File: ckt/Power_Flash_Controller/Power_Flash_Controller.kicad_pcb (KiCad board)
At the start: 2 copper layers, 93 x 67.5 mm, 32 parts, among them J2 Screw_Terminal_01x03, J3 Screw_Terminal_01x03, J4 Screw_Terminal_01x03, K4 SANYOU_SRD_Form_C, K5 SANYOU_SRD_Form_C, K6 SANYOU_SRD_Form_C, M2 MountingHole_2.2mm_M2, Q1 BC857, Q2 BC857, Q3 BC857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

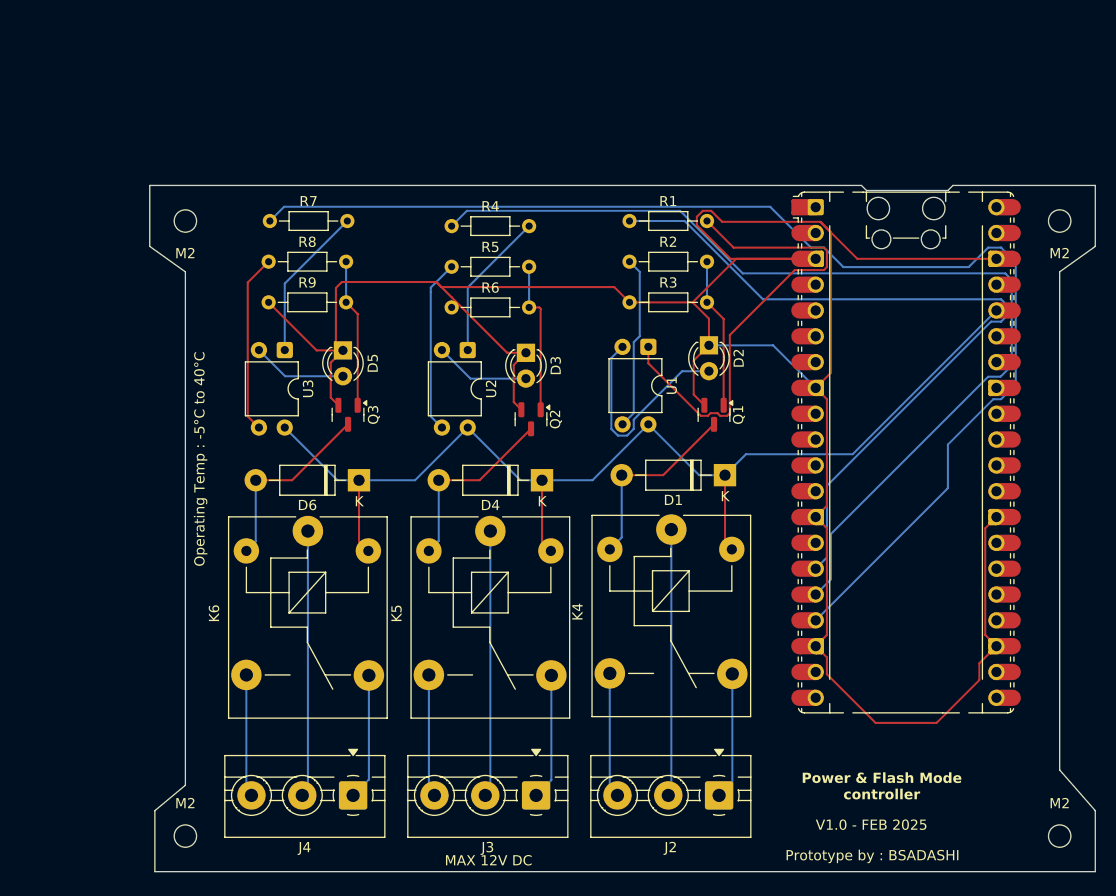
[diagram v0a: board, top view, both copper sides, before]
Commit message: rounded the paths and added GND fill layer
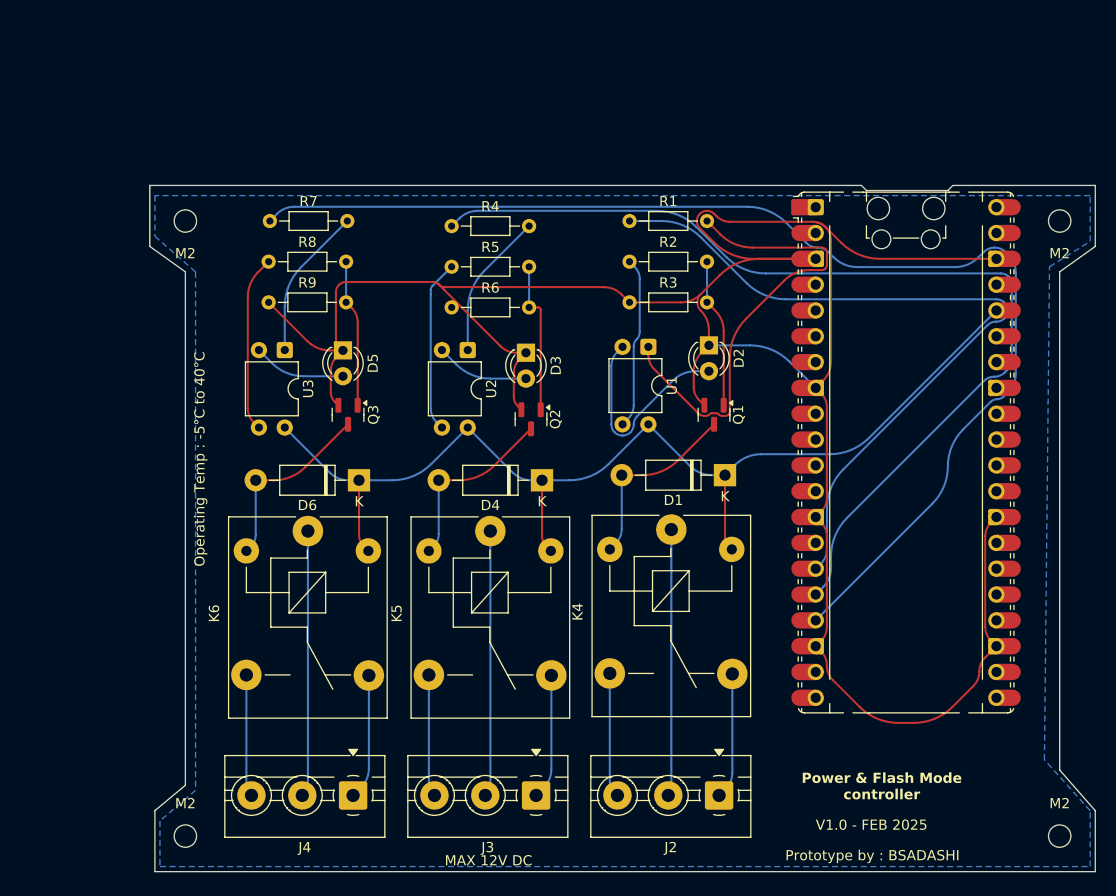
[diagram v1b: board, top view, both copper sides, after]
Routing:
- net GND: track 243.1 -> 238.4 mm
- net /IN3: track 121.6 -> 119.8 mm
- net /PPBus_3p3H: track 109.7 -> 108.0 mm
- net /IN2: track 98.2 -> 96.8 mm
- net /IN1: track 74.9 -> 73.8 mm
- net Net-(R1-Pad2): track 46.7 -> 45.7 mm
- net Net-(D2-A): track 21.6 -> 21.0 mm
- added copper zone on B.Cu, net GND

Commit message: Added connections for Ammeter and Voltmeter
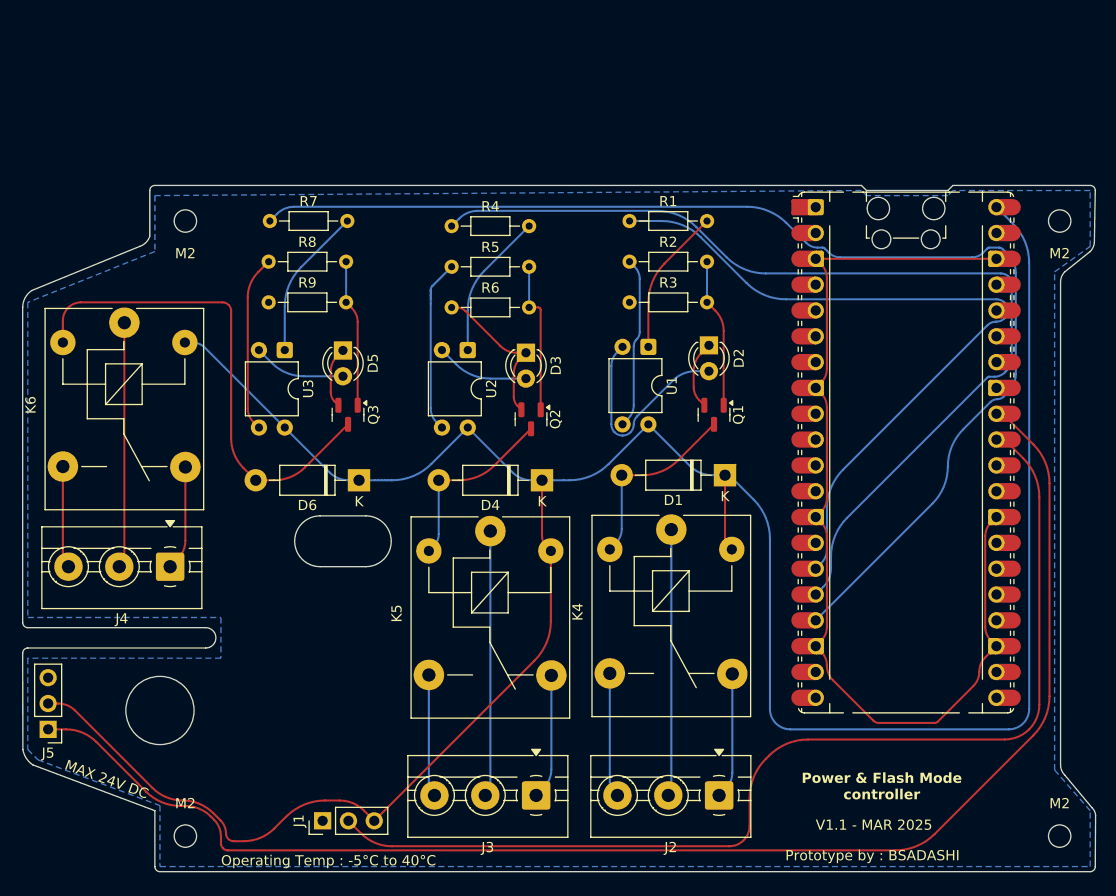
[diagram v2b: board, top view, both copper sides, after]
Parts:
- added J1: Conn_01x03, Connector_PinHeader_2.54mm:PinHeader_1x03_P2.54mm_Vertical, F.Cu at (114.5, 131.0)
- added J5: Conn_01x03, Connector_PinHeader_2.54mm:PinHeader_1x03_P2.54mm_Vertical, F.Cu at (87.5, 122.0)
- moved J4 28.8 mm to (99.5, 106.0)
- moved K6 27.3 mm to (95.0, 82.0)
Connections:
- A1 pad 31: unconnected-(A1-GPIO26_ADC0-Pad31) -> /ADC2Amtr
- A1 pad 32: unconnected-(A1-GPIO27_ADC1-Pad32) -> /ADC2Vmtr
- A1 pad 36: /PPBus_3p3H -> unconnected-(A1-3V3-Pad36)
- A1 pad 40: unconnected-(A1-VBUS-Pad40) -> /PPBus_5p0H
- D1 pad 1: /PPBus_3p3H -> /PPBus_5p0H
- D4 pad 1: /PPBus_3p3H -> /PPBus_5p0H
- D6 pad 1: /PPBus_3p3H -> /PPBus_5p0H
- K4 pad 5: /PPBus_3p3H -> /PPBus_5p0H
- K5 pad 5: /PPBus_3p3H -> /PPBus_5p0H
- K6 pad 5: /PPBus_3p3H -> /PPBus_5p0H
- U1 pad 4: /PPBus_3p3H -> /PPBus_5p0H
- U2 pad 4: /PPBus_3p3H -> /PPBus_5p0H
- U3 pad 4: /PPBus_3p3H -> /PPBus_5p0H
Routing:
- net /PPBus_5p0H: track 0.00 -> 258.2 mm
- net /ADC2Vmtr: track 0.00 -> 140.9 mm
- net GND: track 238.4 -> 125.3 mm
- net /PPBus_3p3H: track 108.0 -> 0.00 mm
- net /ADC2Amtr: track 0.00 -> 104.9 mm
- net Net-(R1-Pad2): track 45.7 -> 14.5 mm
- net Net-(D6-A): track 18.4 -> 48.8 mm
- net /R_NC3: track 12.3 -> 10.3 mm
- net /R_COM3: track 26.2 -> 24.2 mm
- net /R_NO3: track 12.0 -> 10.0 mm
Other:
- board size 93 x 67.5 mm -> 105.5 x 67.5 mm
- board text added: "MAX 24V DC"
- board text added: "V1.1 - MAR 2025"
- board text removed: "MAX 12V DC"
- board text removed: "V1.0 - FEB 2025"

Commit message: added relay no.4 and oled display mount, option for pwm fan and ammeter, voltmeter
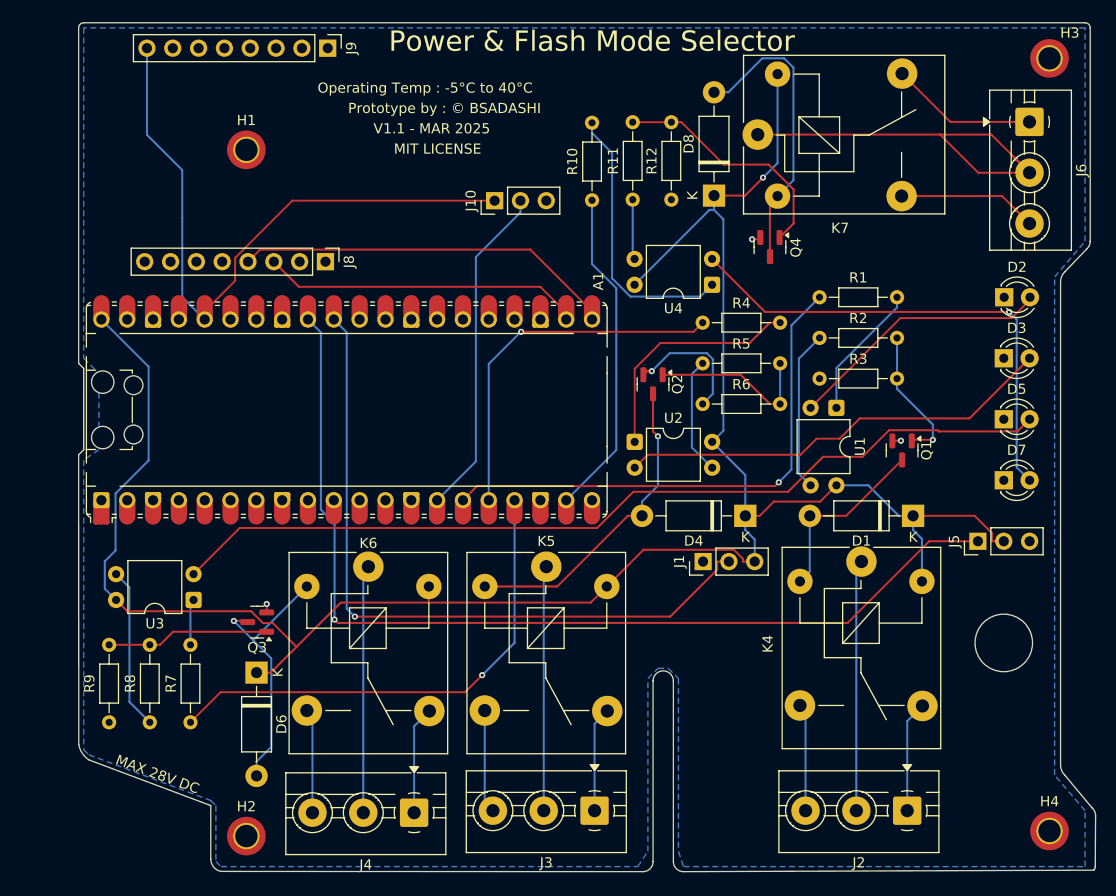
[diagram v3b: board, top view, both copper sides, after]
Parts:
- removed M2 (x4): MountingHole_2.2mm_M2, MountingHole:MountingHole_2.2mm_M2
- added D7: LED, LED_THT:LED_D3.0mm_IRBlack, F.Cu at (181.5, 97.5)
- added D8: 1N4007, Diode_THT:D_DO-41_SOD81_P10.16mm_Horizontal, F.Cu at (153.0, 69.5)
- added H1: MountingHole, MountingHole:MountingHole_2.2mm_M2_DIN965_Pad_TopOnly, F.Cu at (107.0, 65.0)
- added H2: MountingHole, MountingHole:MountingHole_2.2mm_M2_DIN965_Pad_TopOnly, F.Cu at (107.0, 132.5)
- added H3: MountingHole, MountingHole:MountingHole_2.2mm_M2_DIN965_Pad_TopOnly, F.Cu at (186.0, 56.0)
- added H4: MountingHole, MountingHole:MountingHole_2.2mm_M2_DIN965_Pad_TopOnly, F.Cu at (186.0, 132.0)
- added J10: Conn_01x03, Connector_PinHeader_2.54mm:PinHeader_1x03_P2.54mm_Vertical, F.Cu at (131.4, 70.0)
- added J6: Screw_Terminal_01x03, TerminalBlock:TerminalBlock_MaiXu_MX126-5.0-03P_1x03_P5.00mm, F.Cu at (184.0, 62.2)
- added J8: Conn_01x08_Socket, Connector_PinHeader_2.54mm:PinHeader_1x08_P2.54mm_Vertical, F.Cu at (114.8, 76.0)
- added J9: Conn_01x08_Socket, Connector_PinHeader_2.54mm:PinHeader_1x08_P2.54mm_Vertical, F.Cu at (115.0, 55.0)
- added K7: SANYOU_SRD_Form_C, Relay_THT:Relay_SPDT_SANYOU_SRD_Series_Form_C, F.Cu at (157.3, 63.5)
- added Q4: BC857, Package_TO_SOT_SMD:SOT-23, F.Cu at (158.5, 74.6)
- added R10: 330R, Resistor_THT:R_Axial_DIN0204_L3.6mm_D1.6mm_P7.62mm_Horizontal, F.Cu at (141.0, 70.0)
- added R11: 1K, Resistor_THT:R_Axial_DIN0204_L3.6mm_D1.6mm_P7.62mm_Horizontal, F.Cu at (145.0, 69.9)
- added R12: 10K, Resistor_THT:R_Axial_DIN0204_L3.6mm_D1.6mm_P7.62mm_Horizontal, F.Cu at (148.8, 69.9)
- added U4: PC817, Package_DIP:DIP-4_W7.62mm, F.Cu at (152.8, 78.3)
- moved J5 93.3 mm to (179.0, 103.5), turned to 90 degrees
- moved D5 65.4 mm to (181.5, 91.5), turned to 0 degrees
- moved A1 55.2 mm to (116.9, 90.6), turned to 90 degrees
- moved R7 49.9 mm to (101.5, 121.3), turned to 90 degrees
- moved D3 47.0 mm to (181.5, 85.5), turned to 0 degrees
- moved R8 46.8 mm to (97.5, 121.3), turned to 90 degrees
- moved J1 45.3 mm to (151.9, 105.5)
- moved R9 44.2 mm to (93.5, 121.3), turned to 90 degrees
- moved J4 34.1 mm to (123.5, 130.2)
- moved K6 33.9 mm to (119.0, 106.0)
- moved D2 29.4 mm to (181.5, 79.5), turned to 0 degrees
- moved R4 26.5 mm to (151.9, 82.0)
- moved R5 26.5 mm to (151.9, 86.0)
- moved R6 26.5 mm to (151.9, 90.0)
- moved U3 26.2 mm to (101.8, 109.3), turned to 180 degrees
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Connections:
- A1 pad 14: unconnected-(A1-GPIO10-Pad14) -> /PWMFan
- A1 pad 19: unconnected-(A1-GPIO14-Pad19) -> /IN4
- A1 pad 20: unconnected-(A1-GPIO15-Pad20) -> /IN5
- A1 pad 21: unconnected-(A1-GPIO16-Pad21) -> /I2cSDA
- A1 pad 22: unconnected-(A1-GPIO17-Pad22) -> /I2cSCL
- A1 pad 36: unconnected-(A1-3V3-Pad36) -> /PPBus_3p3H
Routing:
- net GND: track 125.3 -> 20.9 mm, vias 0 -> 4
- net Net-(D5-A): track 9.12 -> 88.6 mm
- net /IN3: track 119.4 -> 49.9 mm, vias 0 -> 1
- net /PPBus_3p3H: track 0.00 -> 64.2 mm
- net /IN2: track 96.9 -> 36.9 mm, vias 0 -> 1
- net Net-(D7-A): track 0.00 -> 48.8 mm, vias 0 -> 1
- net /PPBus_5p0H: track 258.2 -> 210.4 mm, vias 0 -> 1
- net /ADC2Vmtr: track 140.9 -> 98.2 mm, vias 0 -> 1
- net /R_COM4: track 0.00 -> 41.1 mm
- net /I2cSDA: track 0.00 -> 38.5 mm
- net /ADC2Amtr: track 104.9 -> 70.4 mm, vias 0 -> 1
- net Net-(D3-A): track 9.20 -> 43.3 mm
- net /PWMFan: track 0.00 -> 33.7 mm
- net /IN4: track 0.00 -> 33.3 mm
- net /I2cSCL: track 0.00 -> 31.7 mm
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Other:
- board size 105.5 x 67.5 mm -> 100 x 83.5 mm
- board text added: "MAX 28V DC"
- board text added: "MIT LICENSE"
- board text added: "Power & Flash Mode Selector"
- board text added: "Prototype by : © BSADASHI"
- board text added: "https://github.com/elementosystems/Rpi-Pico-Relay-Controller"
- board text removed: "MAX 24V DC"
- board text removed: "Power & Flash Mode controller"
- board text removed: "Prototype by : BSADASHI"
